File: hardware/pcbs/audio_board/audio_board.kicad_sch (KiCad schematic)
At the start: 21 parts, among them J1 Header_01x04, J2 MTA100_08, J3 NC3MAH, J4 AudioJack3, J5 NC3MAH, U1 Teensy 4.1

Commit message: WIP on audio board revg schematics
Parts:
- removed J1: Header_01x04, conn:PinHeader_1x04_P2.54mm_Vertical, symbol conn:Conn_01x04
- added J1: Conn_02x06_Odd_Even, conn:PinHeader_2x06_P2.54mm_Vertical, symbol conn:Conn_02x06_Odd_Even
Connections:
- net +3.3V: now also J1.2 (Pin_2)
- net +5V: now also J1.11 (Pin_9)
- net GND: now also J1.12 (Pin_12)
- net I2S1_BCLK: now also J1.7 (Pin_7)
- net I2S1_LRCLK: now also J1.5 (Pin_5)
- net I2S1_MCLK: now also J1.9 (Pin_9)
- net I2S1_RX1: now also J1.3 (Pin_3)
- net I2S1_RX2: now also J1.1 (Pin_1)
- net SCL: now also J1.6 (Pin_6)
- net SDA: now also J1.4 (Pin_4)
- net SPDIF_OUT: now reaches U1.14
- net SPDIF_OUT: now also J1.8 (Pin_8)
- net SPDIF_IN: now reaches U1.15
- net SPDIF_IN: now also J1.10 (Pin_10)
- no-connect marks 22 -> 17

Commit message: prepare for clock fanout
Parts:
- added R10, R11, R12, R2, R3, R4, R5, R6: 47Ω, Resistor_SMD:R_0805_2012Metric, symbol Device:R
- J1: MPN (none) -> 2x PinSocket_1x06; Purpose Pin1 IO2 -> GND; Purpose Pin11 +5V -> +3.3V; Purpose Pin3 IO1 -> IO2; Purpose Pin5 LRCLK -> IO1; Purpose Pin7 BCLK -> LRCLK; Purpose Pin9 MCLK -> BCLK
- renumbered R5 to R13, R6 to R14, R7 to R15, R8 to R16, R9 to R17, R10 to R18, R11 to R19, R2 to R7, R3 to R8, R4 to R9
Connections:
- net +3.3V: now also J1.11 (Pin_9); no longer J1.2 (Pin_2)
- net +5V: now also J1.2 (Pin_2); no longer J1.11 (Pin_9)
- net GND: now also J1.1 (Pin_1)
- net I2S1_BCLK: now also J1.9 (Pin_9); no longer J1.7 (Pin_7), U1.21
- net I2S1_LRCLK: now also J1.7 (Pin_7); no longer J1.5 (Pin_5), U1.20
- net I2S1_MCLK: no longer J1.9 (Pin_9)
- net I2S1_TX1: now also R5.2; no longer U1.7
- net I2S2_BCLK: now also R3.2; no longer U1.4
- net I2S2_FS: now also R2.2; no longer U1.3
- net I2S2_RX: now also R12.2
- net I2S1_RX1: no longer names the net of U1.8
- net I2S1_RX1: now also R6.1; no longer J1.3 (Pin_3)
- net I2S1_RX2: no longer names the net of U1.6
- net I2S1_RX2: now also R4.1; no longer J1.1 (Pin_1)
- new net: R3.1, U1.4
- new net: R10.2, U1.21
- new net: R2.1, U1.3
- new net: R11.2, U1.20
- new net: R5.1, U1.7
- new net ADC/DOUT: R12.1
- new net Clock fanout/BCLK: R10.1
- new net Clock fanout/LRCLK: R11.1
- new net I2S1_IO1: J1.5 (Pin_5), R6.2
- new net I2S1_IO2: J1.3 (Pin_3), R4.2
- no-connect marks 17 -> 18
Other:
- added sheet Clock fanout (clock_fanout.kicad_sch)
- moved on the sheet: J3, J4, J5, R18, R19, U1

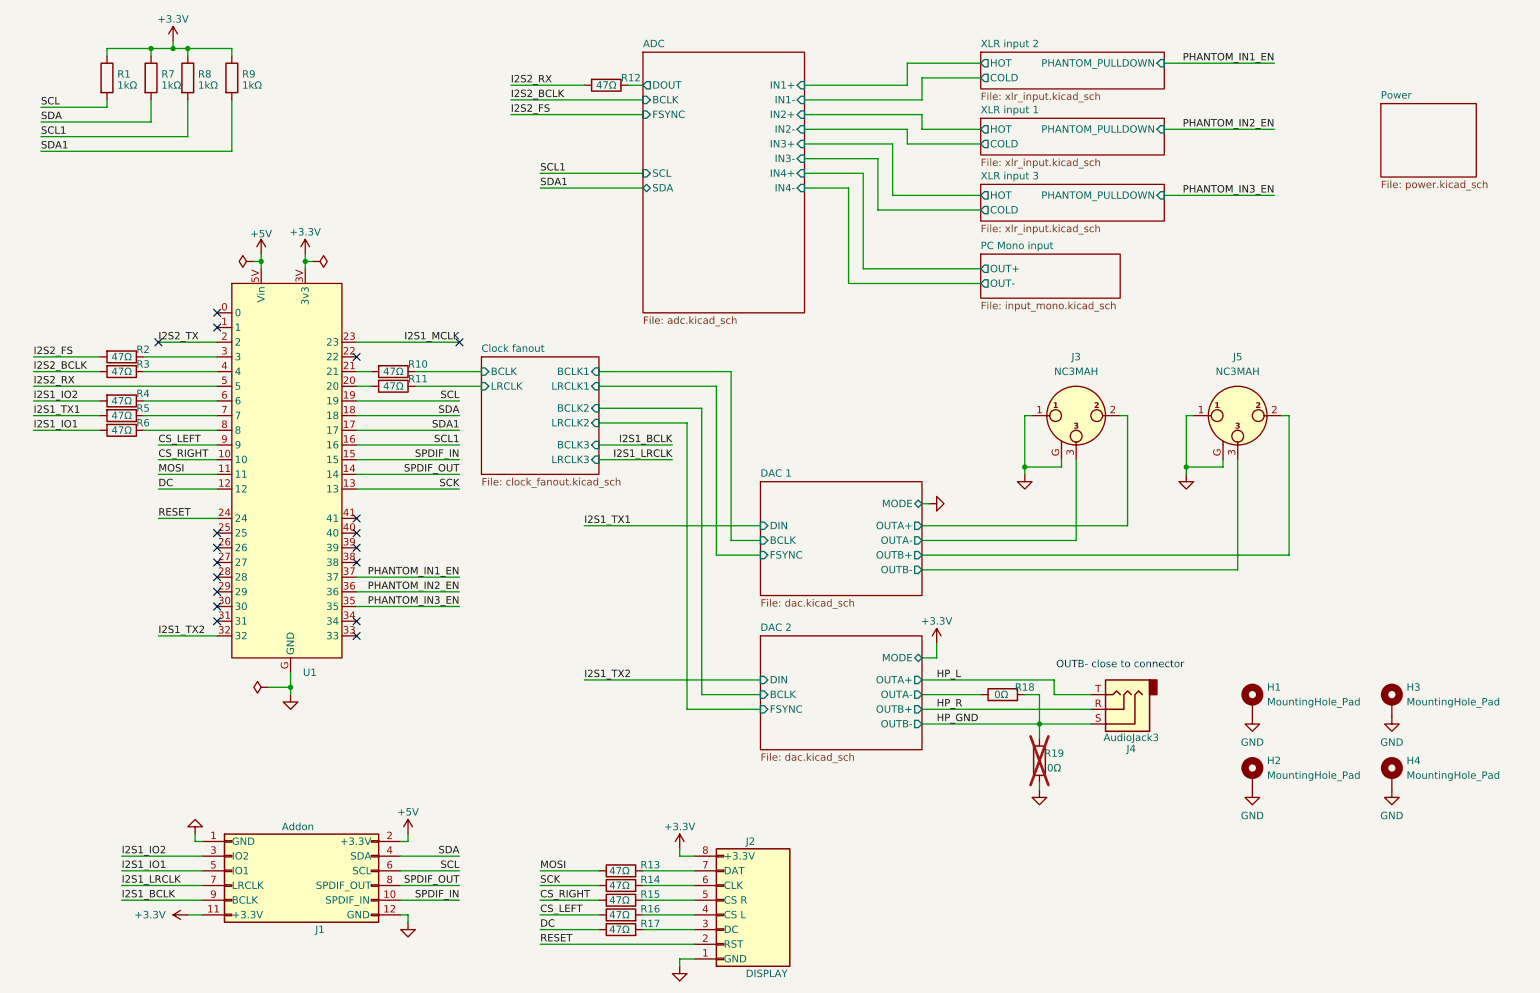
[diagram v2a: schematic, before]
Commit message: audioboard: route clock fanout
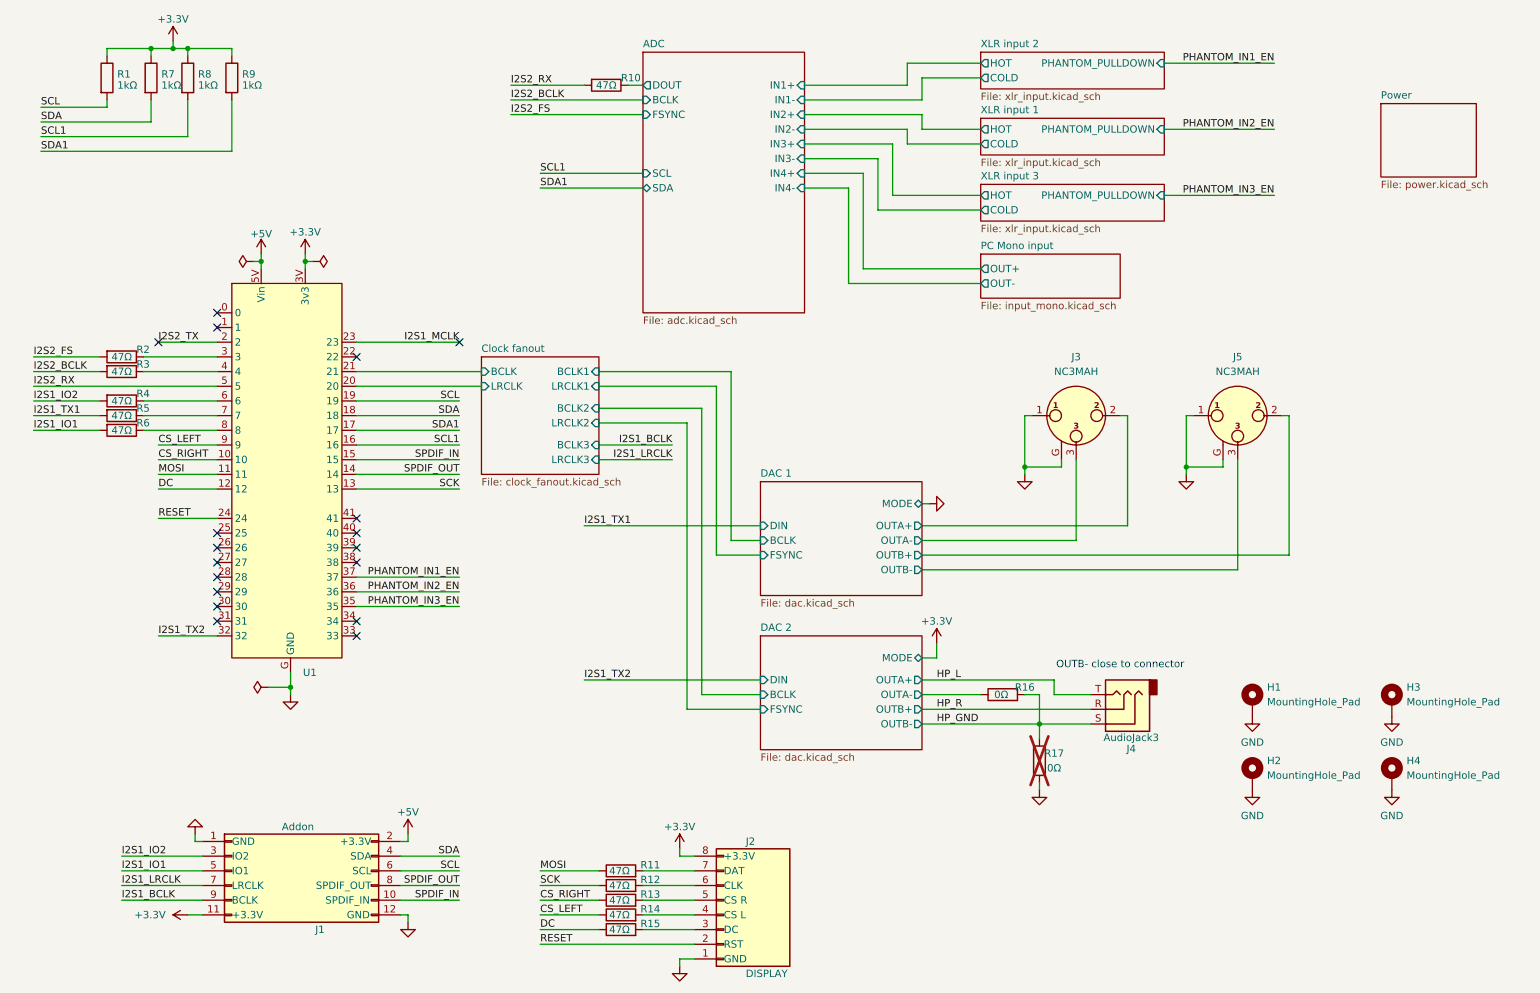
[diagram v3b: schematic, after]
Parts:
- removed R10, R11: 47Ω, Resistor_SMD:R_0805_2012Metric, symbol Device:R
- renumbered R12 to R10, R13 to R11, R14 to R12, R15 to R13, R16 to R14, R17 to R15, R18 to R16, R19 to R17
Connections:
- net Clock fanout/BCLK: now also U1.21
- net Clock fanout/LRCLK: now also U1.20
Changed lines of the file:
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@@
 	(wire
 		(pts
-			(xy 80.01 81.28) (xy 82.55 81.28)
+			(xy 80.01 81.28) (xy 101.6 81.28)
 		)
 		(stroke
@@
 	(wire
 		(pts
-			(xy 80.01 78.74) (xy 82.55 78.74)
+			(xy 80.01 78.74) (xy 101.6 78.74)
 		)
 		(stroke
@@
 	(wire
 		(pts
-			(xy 90.17 78.74) (xy 101.6 78.74)
-		)
-		(stroke
-			(width 0)
-			(type default)
-		)
-	)
-	(wire
-		(pts
 			(xy 80.01 114.3) (xy 97.79 114.3)
 		)
@@
 	(wire
 		(pts
-			(xy 90.17 81.28) (xy 101.6 81.28)
-		)
-		(stroke
-			(width 0)
-			(type default)
-		)
-	)
-	(wire
-		(pts
 			(xy 142.24 110.49) (xy 149.86 110.49)
 		)
@@
 		(in_pos_files yes)
 		(dnp no)
-		(property "Reference" "R12"
+		(property "Reference" "R10"
 			(at 125.73 27.94 90)
 			(show_name no)
@@
 			(project "audio_board"
 				(path "/54443f96-c7c5-4432-b890-45b14a1547a1"
-					(reference "R12")
+					(reference "R10")
 					(unit 1)
 				)
@@
 		(in_pos_files yes)
 		(dnp no)
-		(property "Reference" "R13"
+		(property "Reference" "R11"
 			(at 130.81 164.084 90)
 			(show_name no)
@@
 			(project "audio_board"
 				(path "/54443f96-c7c5-4432-b890-45b14a1547a1"
-					(reference "R13")
+					(reference "R11")
 					(unit 1)
 				)
@@
 	)
 	(symbol
-		(lib_id "Device:R")
-		(at 86.36 78.74 270)
-		(unit 1)
-		(body_style 1)
-		(exclude_from_sim no)
-		(in_bom yes)
-		(on_board yes)
-		(in_pos_files yes)
-		(dnp no)
-		(property "Reference" "R10"
-			(at 88.9 77.47 90)
-			(show_name no)
-			(do_not_autoplace no)
-			(effects
-				(font
-					(size 1.27 1.27)
-				)
-				(justify left)
-			)
-		)
-		(property "Value" "47Ω"
-			(at 86.36 78.74 90)
-			(show_name no)
-			(do_not_autoplace no)
-			(effects
-				(font
-					(size 1.27 1.27)
-				)
-			)
-		)
-		(property "Footprint" "Resistor_SMD:R_0805_2012Metric"
-			(at 86.36 76.962 90)
-			(hide yes)
-			(show_name no)
-			(do_not_autoplace no)
-			(effects
-				(font
-					(size 1.27 1.27)
-				)
-			)
-		)
-		(property "Datasheet" ""
-			(at 86.36 78.74 0)
-			(hide yes)
-			(show_name no)
-			(do_not_autoplace no)
-			(effects
-				(font
-					(size 1.27 1.27)
-				)
-			)
-		)
-		(property "Description" ""
-			(at 86.36 78.74 0)
-			(hide yes)
-			(show_name no)
-			(do_not_autoplace no)
-			(effects
-				(font
-					(size 1.27 1.27)
-				)
-			)
-		)
-		(property "MPN" "R 47Ω 125mW 1% 0805"
-			(at 86.36 78.74 0)
-			(hide yes)
-			(show_name no)
-			(do_not_autoplace no)
-			(effects
-				(font
-					(size 1.27 1.27)
-				)
-			)
-		)
-		(pin "1"
-		)
-		(pin "2"
-		)
-		(instances
-			(project "audio_board"
-				(path "/54443f96-c7c5-4432-b890-45b14a1547a1"
-					(reference "R10")
-					(unit 1)
-				)
-			)
-		)
-	)
-	(symbol
 		(lib_id "power:GND")
 		(at 135.89 181.61 0)
@@
 		(in_pos_files yes)
 		(dnp no)
-		(property "Reference" "R16"
+		(property "Reference" "R14"
 			(at 130.81 171.704 90)
 			(show_name no)
@@
 			(project "audio_board"
 				(path "/54443f96-c7c5-4432-b890-45b14a1547a1"
-					(reference "R16")
+					(reference "R14")
 					(unit 1)
 				)
@@
 		(in_pos_files yes)
 		(dnp no)
-		(property "Reference" "R14"
+		(property "Reference" "R12"
 			(at 130.81 166.624 90)
 			(show_name no)
@@
 			(project "audio_board"
 				(path "/54443f96-c7c5-4432-b890-45b14a1547a1"
-					(reference "R14")
+					(reference "R12")
 					(unit 1)
 				)
@@
 		(in_pos_files yes)
 		(dnp no)
-		(property "Reference" "R18"
+		(property "Reference" "R16"
 			(at 195.58 133.35 90)
 			(show_name no)
@@
 			(project "audio_board"
 				(path "/54443f96-c7c5-4432-b890-45b14a1547a1"
-					(reference "R18")
+					(reference "R16")
 					(unit 1)
 				)
@@
 		(in_pos_files yes)
 		(dnp no)
-		(property "Reference" "R17"
+		(property "Reference" "R15"
 			(at 130.81 174.244 90)
 			(show_name no)
@@
 			(project "audio_board"
 				(path "/54443f96-c7c5-4432-b890-45b14a1547a1"
-					(reference "R17")
+					(reference "R15")
 					(unit 1)
 				)
@@
 		(in_pos_files yes)
 		(dnp no)
-		(property "Reference" "R15"
+		(property "Reference" "R13"
 			(at 130.81 169.164 90)
 			(show_name no)
@@
 			(project "audio_board"
 				(path "/54443f96-c7c5-4432-b890-45b14a1547a1"
-					(reference "R15")
+					(reference "R13")
 					(unit 1)
 				)
@@
 		(in_pos_files yes)
 		(dnp yes)
-		(property "Reference" "R19"
+		(property "Reference" "R17"
 			(at 200.66 144.78 0)
 			(show_name no)
@@
 			(project "audio_board"
 				(path "/54443f96-c7c5-4432-b890-45b14a1547a1"
-					(reference "R19")
+					(reference "R17")
 					(unit 1)
 				)
@@
 					(unit 1)
 				)
-			)
-		)
-	)
-	(symbol
-		(lib_id "Device:R")
-		(at 86.36 81.28 270)
-		(unit 1)
-		(body_style 1)
-		(exclude_from_sim no)
-		(in_bom yes)
-		(on_board yes)
-		(in_pos_files yes)
-		(dnp no)
-		(property "Reference" "R11"
-			(at 88.9 80.01 90)
-			(show_name no)
-			(do_not_autoplace no)
-			(effects
-				(font
-					(size 1.27 1.27)
-				)
-				(justify left)
-			)
-		)
-		(property "Value" "47Ω"
-			(at 86.36 81.28 90)
-			(show_name no)
-			(do_not_autoplace no)
-			(effects
-				(font
-					(size 1.27 1.27)
-				)
-			)
-		)
-		(property "Footprint" "Resistor_SMD:R_0805_2012Metric"
-			(at 86.36 79.502 90)
-			(hide yes)
-			(show_name no)
-			(do_not_autoplace no)
-			(effects
-				(font
-					(size 1.27 1.27)
-				)
-			)
-		)
-		(property "Datasheet" ""
-			(at 86.36 81.28 0)
-			(hide yes)
-			(show_name no)
-			(do_not_autoplace no)
-			(effects
-				(font
-					(size 1.27 1.27)
-				)
-			)
-		)
-		(property "Description" ""
-			(at 86.36 81.28 0)
-			(hide yes)
-			(show_name no)
-			(do_not_autoplace no)
-			(effects
-				(font
-					(size 1.27 1.27)
-				)
-			)
-		)
-		(property "MPN" "R 47Ω 125mW 1% 0805"
-			(at 86.36 81.28 0)
-			(hide yes)
-			(show_name no)
-			(do_not_autoplace no)
-			(effects
-				(font
-					(size 1.27 1.27)
-				)
-			)
-		)
-		(pin "1"
-		)
-		(pin "2"
-		)
-		(instances
-			(project "audio_board"
-				(path "/54443f96-c7c5-4432-b890-45b14a1547a1"
-					(reference "R11")
-					(unit 1)
-				)

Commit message: audioboard: finalise routing
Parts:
- removed H1, H2, H3, H4: MountingHole_Pad, MountingHole:MountingHole_3.2mm_M3_Pad_Via, symbol Mechanical:MountingHole_Pad
- removed J1: Conn_02x06_Odd_Even, conn:PinHeader_2x06_P2.54mm_Vertical, symbol conn:Conn_02x06_Odd_Even
- added J1: Conn_02x07_Odd_Even, conn:PinHeader_2x07_P2.54mm_Vertical, symbol conn:Conn_02x07_Odd_Even
- added R7, R8: 47Ω, Resistor_SMD:R_0805_2012Metric, symbol Device:R
- renumbered R8 to R10, R9 to R11, R10 to R12, R11 to R13, R12 to R14, R13 to R15, R14 to R16, R15 to R17, R16 to R18, R17 to R19, R7 to R9
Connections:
- net +3.3V: now also J1.13 (Pin_9), J1.14 (Pin_12)
- net +5V: now also J1.12 (Pin_12)
- net GND: now also J1.1 (Pin_1), J1.2 (Pin_2)
- net I2S1_BCLK: now also J1.11 (Pin_9)
- net I2S1_LRCLK: now also J1.9 (Pin_9)
- net I2S1_TX2: now also R8.2; no longer U1.32
- net SCL: now also J1.10 (Pin_10)
- net SDA: now also J1.8 (Pin_8)
- net SPDIF_IN: now also J1.4 (Pin_4)
- net SPDIF_OUT: now also J1.6 (Pin_6)
- net DISP_DC: now reaches J2.3 (Pin_3), R17.2
- net DISP_CS_LEFT: now reaches J2.4 (Pin_4), R16.2
- net DISP_CS_RIGHT: now reaches J2.5 (Pin_5), R15.2
- net DISP_SCK: now reaches J2.6 (Pin_6), R14.2
- net DISP_MOSI: now reaches J2.7 (Pin_7), R13.2
- net at U1.31: now also R16.1
- net I2S1_RX1: now reaches R4.1, U1.6
- net I2S1_RX2: now reaches R6.1, U1.8
- net CS_LEFT: no longer names the net of U1.9
- net CS_LEFT: now also R7.1; no longer R16.1
- net CS_RIGHT: no longer names the net of R15.1, U1.10
- net DC: no longer names the net of R17.1, U1.12
- net I2S1_IO1: no longer names the net of R6.2
- net I2S1_IO1: now also J1.5 (Pin_5)
- net I2S1_IO2: no longer names the net of R4.2
- net I2S1_IO2: now also J1.7 (Pin_7)
- net MOSI: no longer names the net of R13.1, U1.11
- net RESET renamed DISP_RST
- net SCK: no longer names the net of R14.1, U1.13
- new net: R8.1, U1.32
- new net I2S1_TX3: J1.3 (Pin_3), R7.2
- no-connect marks 18 -> 17
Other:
- added sheet Mechanics (mechanics.kicad_sch)
- moved on the sheet: J3, J4, J5, R13, R14, R15, R16, R17, R18, R19, R2, R3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

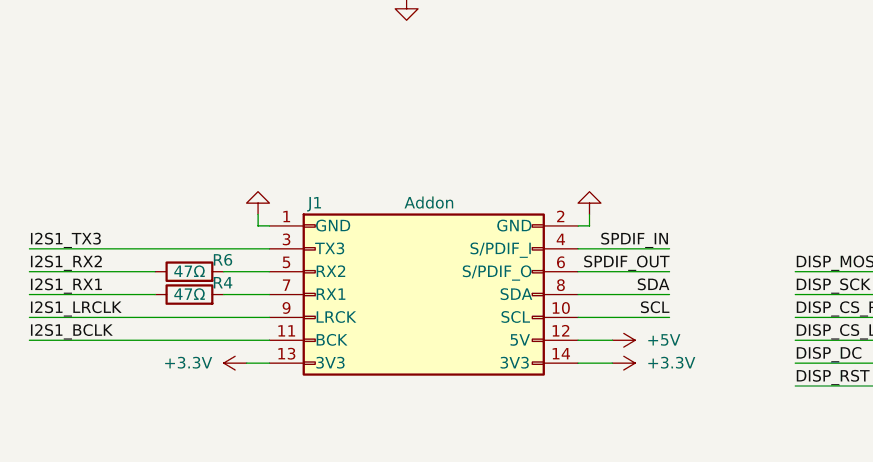
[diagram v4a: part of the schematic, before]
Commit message: rearrange addon header
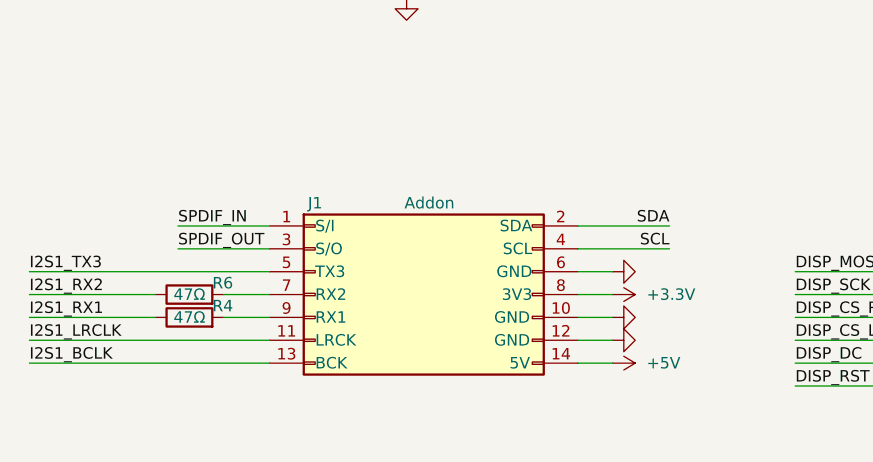
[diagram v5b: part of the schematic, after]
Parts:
- J1: Purpose Pin1 GND -> S/I; Purpose Pin10 SCL -> GND; Purpose Pin11 BCK -> LRCK; Purpose Pin12 5V -> GND; Purpose Pin13 3V3 -> BCK; Purpose Pin14 3V3 -> 5V; Purpose Pin2 GND -> SDA; Purpose Pin3 TX3 -> S/O; Purpose Pin4 S/PDIF_I -> SCL; Purpose Pin5 RX2 -> TX3; Purpose Pin6 S/PDIF_O -> GND; Purpose Pin7 RX1 -> RX2; Purpose Pin8 SDA -> 3V3; Purpose Pin9 LRCK -> RX1
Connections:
- net +3.3V: now also J1.8 (Pin_8); no longer J1.13 (Pin_9), J1.14 (Pin_12)
- net +5V: now also J1.14 (Pin_12); no longer J1.12 (Pin_12)
- net GND: now also J1.10 (Pin_10), J1.12 (Pin_12), J1.6 (Pin_6); no longer J1.1 (Pin_1), J1.2 (Pin_2)
- net I2S1_BCLK: now also J1.13 (Pin_9); no longer J1.11 (Pin_9)
- net I2S1_LRCLK: now also J1.11 (Pin_9); no longer J1.9 (Pin_9)
- net I2S1_TX3: now also J1.5 (Pin_5); no longer J1.3 (Pin_3)
- net SCL: now also J1.4 (Pin_4); no longer J1.10 (Pin_10)
- net SDA: now also J1.2 (Pin_2); no longer J1.8 (Pin_8)
- net SPDIF_IN: now also J1.1 (Pin_1); no longer J1.4 (Pin_4)
- net SPDIF_OUT: now also J1.3 (Pin_3); no longer J1.6 (Pin_6)
- net at R4.2: now also J1.9 (Pin_9); no longer J1.7 (Pin_7)
- net at R6.2: now also J1.7 (Pin_7); no longer J1.5 (Pin_5)
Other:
- moved on the sheet: R4, R6

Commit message: minor changes to audioboard
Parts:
- removed R4, R6: 47Ω, Resistor_SMD:R_0805_2012Metric, symbol Device:R
- renumbered R16 to R10, R8 to R11, R10 to R12, R11 to R13, R12 to R15, R18 to R16, R19 to R17, R9 to R2, R2 to R3, R3 to R4, R7 to R6, R15 to R7, R13 to R8, R17 to R9
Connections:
- net I2S1_RX1: now also J1.9 (Pin_9)
- net I2S1_RX2: now also J1.7 (Pin_7)
